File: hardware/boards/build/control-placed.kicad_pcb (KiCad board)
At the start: 4 copper layers, 177.9 x 107.5 mm, 108 parts

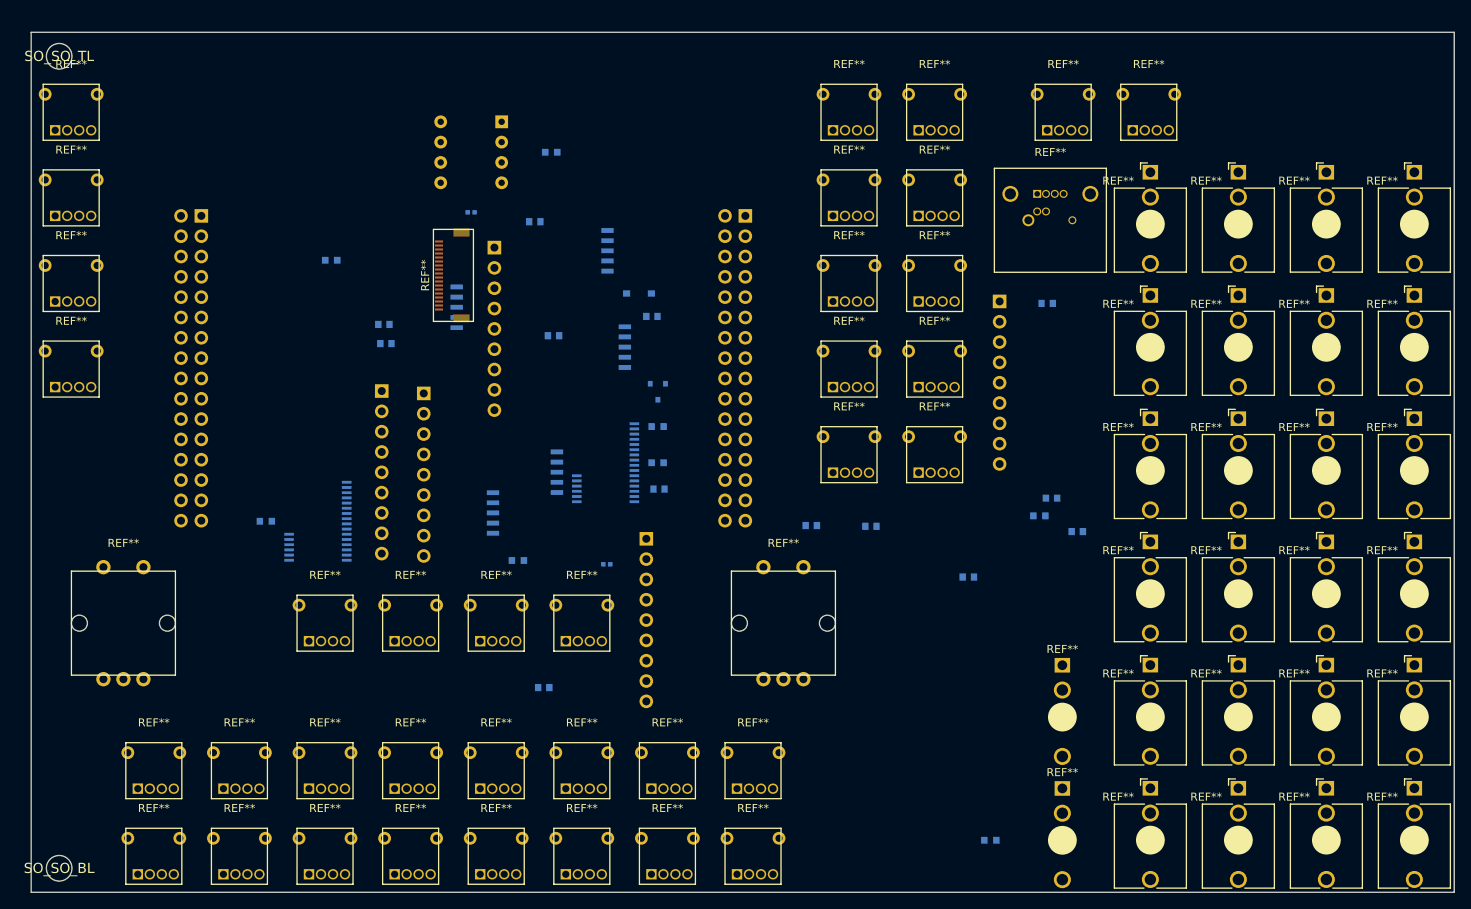
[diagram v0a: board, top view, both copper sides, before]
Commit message: Parts replaced
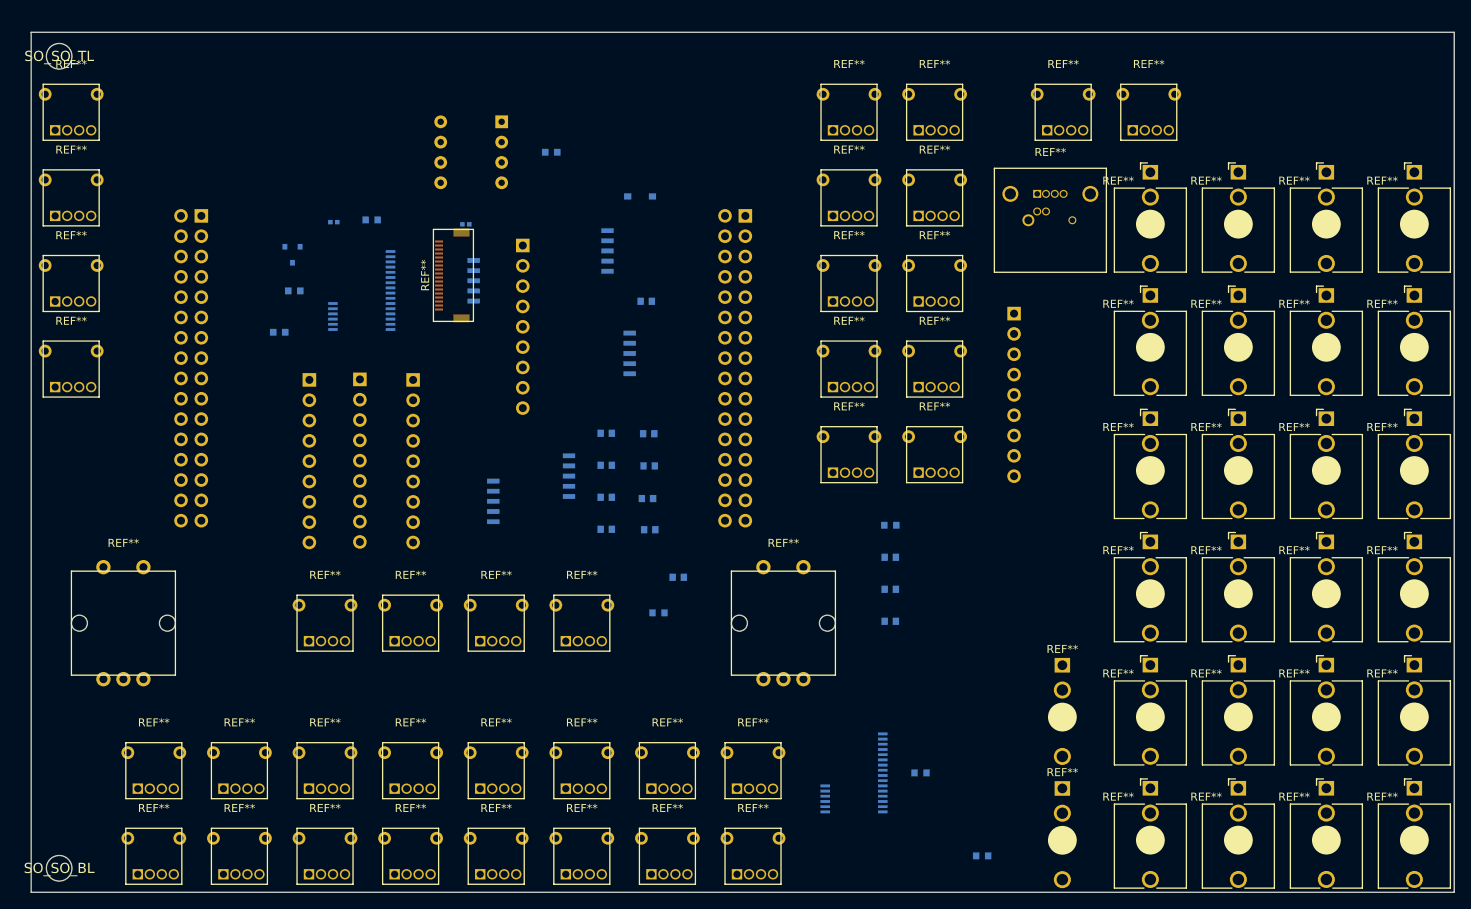
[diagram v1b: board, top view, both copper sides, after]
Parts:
- removed the REF** at (139.9, 63.7)
- removed the REF** at (161.9, 17.5)
- removed the REF** at (161.9, 79.1)
- removed the REF** at (139.9, 32.9)
- removed the REF** at (172.9, 48.3)
- removed the REF** at (139.9, 79.1)
- removed the REF** at (161.9, 94.5)
- removed the REF** at (150.9, 94.5)
- removed the REF** at (161.9, 32.9)
- removed the REF** at (139.9, 94.5)
- removed the REF** at (150.9, 63.7)
- removed the REF** at (172.9, 79.1)
- removed the REF** at (172.9, 17.5)
- removed the REF** at (139.9, 17.5)
- removed the REF** at (150.9, 32.9)
- removed the REF** at (150.9, 79.1)
- removed the REF** at (150.9, 48.3)
- removed the REF** at (161.9, 63.7)
- removed the REF** at (172.9, 32.9)
- removed the REF** at (161.9, 48.3)
- removed the REF** at (150.9, 17.5)
- removed the REF** at (172.9, 94.5)
- removed the REF** at (139.9, 48.3)
- removed the REF** at (121.1, 33.6)
- removed the REF** at (71.8, 53.8)
- removed the REF** at (71.5, 41.3)
- removed the REF** at (55.0, 62.0)
- removed the REF** at (57.9, 26.9)
- removed the REF** at (63.0, 56.9)
- removed the REF** at (76.9, 63.3)
- removed the REF** at (49.1, 45.1)
- removed the REF** at (50.5, 36.3)
- removed the REF** at (172.9, 63.7)
- removed the REF** at (35.8, 61.1)
- removed the REF** at (69.3, 29.2)
- removed the REF** at (43.8, 44.8)
- added REF**: WQP518MA, WQP518MA:WQP518MA, F.Cu at (150.9, 32.9)
- added REF**: WQP518MA, WQP518MA:WQP518MA, F.Cu at (139.9, 48.3)
- added REF**: WQP518MA, WQP518MA:WQP518MA, F.Cu at (139.9, 63.7)
- added REF**: WQP518MA, WQP518MA:WQP518MA, F.Cu at (172.9, 17.5)
- added REF**: WQP518MA, WQP518MA:WQP518MA, F.Cu at (139.9, 32.9)
- added REF**: WQP518MA, WQP518MA:WQP518MA, F.Cu at (150.9, 17.5)
- added REF**: WQP518MA, WQP518MA:WQP518MA, F.Cu at (139.9, 94.5)
- added REF**: WQP518MA, WQP518MA:WQP518MA, F.Cu at (172.9, 94.5)
- added REF**: WQP518MA, WQP518MA:WQP518MA, F.Cu at (150.9, 79.1)
- added REF**: WQP518MA, WQP518MA:WQP518MA, F.Cu at (161.9, 32.9)
- added REF**: WQP518MA, WQP518MA:WQP518MA, F.Cu at (161.9, 17.5)
- added REF**: WQP518MA, WQP518MA:WQP518MA, F.Cu at (161.9, 48.3)
- added REF**: WQP518MA, WQP518MA:WQP518MA, F.Cu at (139.9, 17.5)
- added REF**: WQP518MA, WQP518MA:WQP518MA, F.Cu at (172.9, 32.9)
- added REF**: WQP518MA, WQP518MA:WQP518MA, F.Cu at (161.9, 94.5)
- added REF**: WQP518MA, WQP518MA:WQP518MA, F.Cu at (172.9, 79.1)
- added REF**: WQP518MA, WQP518MA:WQP518MA, F.Cu at (172.9, 48.3)
- added REF**: WQP518MA, WQP518MA:WQP518MA, F.Cu at (150.9, 94.5)
- added REF**: WQP518MA, WQP518MA:WQP518MA, F.Cu at (161.9, 79.1)
- added REF**: WQP518MA, WQP518MA:WQP518MA, F.Cu at (161.9, 63.7)
- added REF**: WQP518MA, WQP518MA:WQP518MA, F.Cu at (150.9, 48.3)
- added REF**: WQP518MA, WQP518MA:WQP518MA, F.Cu at (172.9, 63.7)
- added REF**: WQP518MA, WQP518MA:WQP518MA, F.Cu at (139.9, 79.1)
- added REF**: WQP518MA, WQP518MA:WQP518MA, F.Cu at (150.9, 63.7)
- added REF**: SOIC-16, 74HC165D:SOIC-16, B.Cu at (69.3, 29.2)
- added REF**: SIP-9, ResistorNetwork9:SIP-9, B.Cu at (34.8, 43.5)
- added REF**: SOIC-16, 74HC165D:SOIC-16, B.Cu at (55.1, 60.5)
- added REF**: HTSSOP-32, TLC5947DAP:HTSSOP-32, B.Cu at (102.9, 92.6)
- added REF**: SIP-9, ResistorNetwork9:SIP-9, B.Cu at (41.1, 43.4)
- added REF**: SOIC-16, 74HC165D:SOIC-16, B.Cu at (64.5, 57.4)
- added REF**: SIP-9, ResistorNetwork9:SIP-9, B.Cu at (122.9, 35.2)
- added REF**: SOIC-16, 74HC165D:SOIC-16, B.Cu at (52.6, 33.0)
- added REF**: SOIC-16, 74HC165D:SOIC-16, B.Cu at (72.1, 42.1)
- added REF**: SIP-9, ResistorNetwork9:SIP-9, B.Cu at (47.7, 43.5)
- added REF**: HTSSOP-32, TLC5947DAP:HTSSOP-32, B.Cu at (41.3, 32.3)
- added REF**: SIP-9, ResistorNetwork9:SIP-9, B.Cu at (61.5, 26.7)
- C1, C10, C11, C12, C13, C2, C3, C4, C5, C7, C8, C9: value 0F -> 100nF
- C6: value 0F -> 10µF
- R1, R2: value 2000Ω -> 2kΩ
- R10: value 10000Ω -> 10kΩ
- R3: value 4700Ω -> 4.7kΩ
- R9: value 100000Ω -> 100kΩ
- moved C6 61.1 mm to (76.9, 33.6)
- moved R9 54.7 mm to (37.8, 23.7)
- moved R2 50.8 mm to (111.2, 92.6)
- moved C12 50.4 mm to (77.3, 62.2)
- moved REF** 48.8 mm to (32.7, 27.8)
- moved R8 48.8 mm to (31.0, 37.5)
- moved C2 37.3 mm to (107.4, 65.6)
- moved C3 35.8 mm to (77.2, 50.2)
- moved C7 33.1 mm to (71.9, 62.1)
- moved C10 32.8 mm to (80.9, 68.1)
- moved C9 31.5 mm to (107.4, 69.6)
- moved C1 31.5 mm to (71.9, 54.1)
- moved R1 29.0 mm to (32.9, 32.3)
- moved C8 27.9 mm to (71.9, 50.1)
- moved C13 25.0 mm to (71.9, 58.1)
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
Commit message: Update parts and placement algos
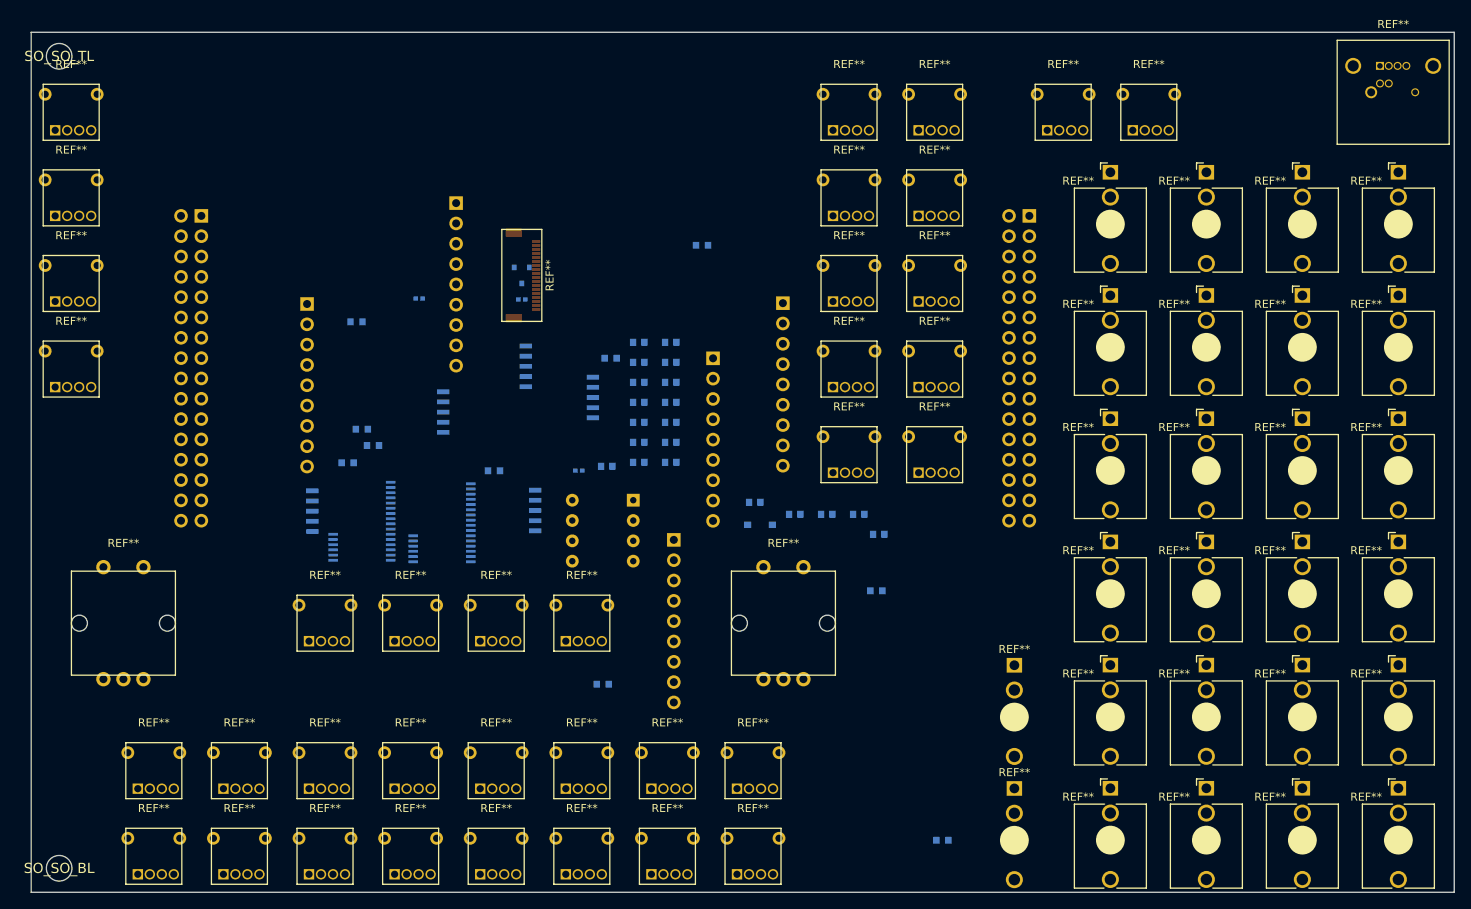
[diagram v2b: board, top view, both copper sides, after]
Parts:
- removed the REF** at (150.9, 32.9)
- removed the REF** at (139.9, 48.3)
- removed the REF** at (139.9, 63.7)
- removed the REF** at (172.9, 17.5)
- removed the REF** at (139.9, 32.9)
- removed the REF** at (150.9, 17.5)
- removed the REF** at (139.9, 94.5)
- removed the REF** at (172.9, 94.5)
- removed the REF** at (150.9, 79.1)
- removed the REF** at (161.9, 32.9)
- removed the REF** at (161.9, 17.5)
- removed the REF** at (128.9, 85.6)
- removed the REF** at (161.9, 48.3)
- removed the REF** at (139.9, 17.5)
- removed the REF** at (172.9, 32.9)
- removed the REF** at (161.9, 94.5)
- removed the REF** at (172.9, 79.1)
- removed the REF** at (172.9, 48.3)
- removed the REF** at (128.9, 101.0)
- removed the REF** at (150.9, 94.5)
- removed the REF** at (161.9, 79.1)
- removed the REF** at (161.9, 63.7)
- removed the REF** at (150.9, 48.3)
- removed the REF** at (172.9, 63.7)
- removed the REF** at (139.9, 79.1)
- removed the REF** at (150.9, 63.7)
- removed the REF** at (69.3, 29.2)
- removed the REF** at (34.8, 43.5)
- removed the REF** at (55.1, 60.5)
- removed the REF** at (102.9, 92.6)
- removed the REF** at (41.1, 43.4)
- removed the REF** at (64.5, 57.4)
- removed the REF** at (122.9, 35.2)
- removed the REF** at (52.6, 33.0)
- removed the REF** at (72.1, 42.1)
- removed the REF** at (47.7, 43.5)
- removed the REF** at (41.3, 32.3)
- removed the REF** at (61.5, 26.7)
- added C14: 100nF, YAGEO_CC0603KRX7R9BB104:C0603, B.Cu at (75.9, 51.2)
- added C15: 100nF, YAGEO_CC0603KRX7R9BB104:C0603, B.Cu at (103.4, 60.2)
- added C16: 100nF, YAGEO_CC0603KRX7R9BB104:C0603, B.Cu at (75.9, 41.2)
- added C17: 10µF, Samsung_Electro_Mechanics_CL10A106KP8NNNC:C0603, B.Cu at (75.9, 43.8)
- added C18: 10µF, Samsung_Electro_Mechanics_CL10A106KP8NNNC:C0603, B.Cu at (75.9, 46.2)
- added C19: 100nF, YAGEO_CC0603KRX7R9BB104:C0603, B.Cu at (75.9, 48.8)
- added C20: 100nF, YAGEO_CC0603KRX7R9BB104:C0603, B.Cu at (79.9, 53.8)
- added R11: 100kΩ, UNI_ROYAL_0402WGF1003TCE:R0402, B.Cu at (48.5, 33.3)
- added R12: 10kΩ, UNI_ROYAL_0603WAF1002T5E:R0603, B.Cu at (72.4, 40.8)
- added R13: 47kΩ, UNI_ROYAL_0603WAF4702T5E:R0603, B.Cu at (83.9, 26.6)
- added REF**: WQP518MA, WQP518MA:WQP518MA, F.Cu at (170.9, 32.9)
- added REF**: WQP518MA, WQP518MA:WQP518MA, F.Cu at (158.9, 79.1)
- added REF**: WQP518MA, WQP518MA:WQP518MA, F.Cu at (158.9, 32.9)
- added REF**: WQP518MA, WQP518MA:WQP518MA, F.Cu at (134.9, 79.1)
- added REF**: WQP518MA, WQP518MA:WQP518MA, F.Cu at (146.9, 32.9)
- added REF**: WQP518MA, WQP518MA:WQP518MA, F.Cu at (146.9, 94.5)
- added REF**: WQP518MA, WQP518MA:WQP518MA, F.Cu at (158.9, 48.3)
- added REF**: WQP518MA, WQP518MA:WQP518MA, F.Cu at (134.9, 17.5)
- added REF**: WQP518MA, WQP518MA:WQP518MA, F.Cu at (146.9, 79.1)
- added REF**: WQP518MA, WQP518MA:WQP518MA, F.Cu at (134.9, 94.5)
- added REF**: PJ366ST, PJ366ST:PJ366ST, F.Cu at (122.9, 101.0)
- added REF**: WQP518MA, WQP518MA:WQP518MA, F.Cu at (170.9, 17.5)
- added REF**: WQP518MA, WQP518MA:WQP518MA, F.Cu at (134.9, 48.3)
- added REF**: WQP518MA, WQP518MA:WQP518MA, F.Cu at (170.9, 63.7)
- added REF**: WQP518MA, WQP518MA:WQP518MA, F.Cu at (146.9, 63.7)
- added REF**: WQP518MA, WQP518MA:WQP518MA, F.Cu at (170.9, 79.1)
- added REF**: WQP518MA, WQP518MA:WQP518MA, F.Cu at (158.9, 94.5)
- added REF**: WQP518MA, WQP518MA:WQP518MA, F.Cu at (170.9, 48.3)
- added REF**: WQP518MA, WQP518MA:WQP518MA, F.Cu at (158.9, 17.5)
- added REF**: WQP518MA, WQP518MA:WQP518MA, F.Cu at (146.9, 17.5)
- added REF**: PJ366ST, PJ366ST:PJ366ST, F.Cu at (122.9, 85.6)
- added REF**: WQP518MA, WQP518MA:WQP518MA, F.Cu at (134.9, 32.9)
- added REF**: WQP518MA, WQP518MA:WQP518MA, F.Cu at (146.9, 48.3)
- added REF**: WQP518MA, WQP518MA:WQP518MA, F.Cu at (158.9, 63.7)
- added REF**: SOIC-16, 74HC165D:SOIC-16, B.Cu at (48.8, 49.4)
- added REF**: HTSSOP-32, TLC5947DAP:HTSSOP-32, B.Cu at (51.4, 61.3)
- added REF**: SOIC-16, 74HC165D:SOIC-16, B.Cu at (59.1, 43.7)
- added REF**: SIP-9, ResistorNetwork9:SIP-9, B.Cu at (53.1, 21.4)
- added REF**: HTSSOP-32, TLC5947DAP:HTSSOP-32, B.Cu at (41.3, 61.1)
- added REF**: SIP-9, ResistorNetwork9:SIP-9, B.Cu at (80.3, 63.4)
- added REF**: SIP-9, ResistorNetwork9:SIP-9, B.Cu at (85.2, 40.8)
- added REF**: SIP-9, ResistorNetwork9:SIP-9, B.Cu at (94.0, 33.9)
- added REF**: SOIC-16, 74HC165D:SOIC-16, B.Cu at (60.3, 61.7)
- added REF**: SOIC-16, 74HC165D:SOIC-16, B.Cu at (67.5, 47.6)
- added REF**: WQP518MA, WQP518MA:WQP518MA, F.Cu at (134.9, 63.7)
- added REF**: SOIC-16, 74HC165D:SOIC-16, B.Cu at (32.4, 61.8)
- added REF**: SIP-9, ResistorNetwork9:SIP-9, B.Cu at (34.5, 34.0)
- added REF**: WQP518MA, WQP518MA:WQP518MA, F.Cu at (170.9, 94.5)
- R1: value 2kΩ -> 10kΩ; footprint UNI_ROYAL_0603WAF2001T5E:R0603 -> UNI_ROYAL_0603WAF1002T5E:R0603
- R10: value 10kΩ -> 33Ω; footprint UNI_ROYAL_0603WAF1002T5E:R0603 -> UNI_ROYAL_0402WGF330JTCE:R0402
- R3: value 4.7kΩ -> 2kΩ; footprint UNI_ROYAL_0402WGF4701TCE:R0402 -> UNI_ROYAL_0603WAF2001T5E:R0603
- R4: value 220Ω -> 4.7kΩ; footprint UNI_ROYAL_0603WAF2200T5E:R0603 -> UNI_ROYAL_0402WGF4701TCE:R0402
- R7: value 470Ω -> 220Ω; footprint UNI_ROYAL_0603WAF4700T5E:R0603 -> UNI_ROYAL_0603WAF2200T5E:R0603
- R8: value 100Ω -> 1kΩ; footprint UNI_ROYAL_0603WAF1000T5E:R0603 -> UNI_ROYAL_0603WAF1001T5E:R0603
- R9: value 100kΩ -> 100Ω; footprint UNI_ROYAL_0402WGF1003TCE:R0402 -> UNI_ROYAL_0603WAF1000T5E:R0603
- moved R2 82.0 mm to (41.3, 49.6)
- moved R7 64.8 mm to (71.5, 81.5)
- moved R10 54.0 mm to (61.3, 33.4)
- moved REF** 50.1 mm to (71.5, 62.3)
- moved REF** 45.7 mm to (170.2, 7.50)
- moved R6 45.5 mm to (113.9, 101.0)
- moved C11 44.4 mm to (79.9, 38.8)
- moved REF** 43.7 mm to (91.1, 61.6)
- moved R4 39.9 mm to (68.5, 54.8)
- moved C9 38.6 mm to (71.9, 54.2)
- moved C8 36.3 mm to (105.9, 62.8)
- moved R5 35.7 mm to (105.6, 69.8)
- moved REF** 35.5 mm to (123.5, 42.0)
- moved C2 35.1 mm to (79.9, 43.8)
- moved C6 32.5 mm to (95.4, 60.2)
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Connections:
- C10 pad 1: c_sd-power-hv -> c_cv_c-power-hv
- C11 pad 1: c_sd-power-hv -> c_cv_d-power-hv
- C12 pad 1: c_sd-power-hv -> c_lcd_rst-power-hv
- C8 pad 1: c_lcd_rst-power-hv -> c_cv_a-power-hv
- C9 pad 1: c_sd-power-hv -> c_cv_b-power-hv
- R1 pad 1: IREF -> c_sd-power-hv
- R1 pad 2: lv -> BLANK
- R10 pad 2: c_lcd_rst-power-hv -> 10
- R2 pad 1: leds-IREF -> IREF
- R3 pad 1: VE -> leds-IREF
- R4 pad 1: TIP -> VE
- R4 pad 2: CATHODE -> lv
- R5 pad 1: c_sd-power-hv -> TIP
- R5 pad 2: RING -> CATHODE
- R6 pad 1: midi_tx -> hv
- R6 pad 2: midi-TIP -> RING
- R7 pad 1: c_sd-power-hv -> midi_tx
- R7 pad 2: midi_rx -> midi-TIP
- R8 pad 1: lcd_bl -> c_sd-power-hv
- R8 pad 2: gate -> midi_rx
- R9 pad 1: gate -> lcd_bl
- R9 pad 2: lv -> gate
- REF** pad 10: c_sd-power-hv -> 10
- REF** pad 10: cv_a -> c_cv_c-power-hv
- REF** pad 11: cv_b -> c_cv_d-power-hv
- REF** pad 12: cv_c -> lv
- REF** pad 13: cv_d -> gate1
- REF** pad 14: gate1 -> gate2
- REF** pad 15: gate2 -> gate3
- REF** pad 16: gate3 -> gate4
- REF** pad 17: gate4 -> lv
- REF** pad 22: vel1 -> lv
- REF** pad 23: vel2 -> vel1
- REF** pad 24: vel3 -> vel2
- REF** pad 25: vel4 -> vel3
- REF** pad 26: mod1 -> vel4
- REF** pad 27: mod2 -> lv
- REF** pad 28: mod3 -> mod1
- REF** pad 29: mod4 -> mod2
- REF** pad 3: A-1 -> clk_in
- REF** pad 30: hv -> mod3
- REF** pad 31: lv -> mod4
- REF** pad 4: B-1 -> clk_out
- REF** pad 5: enc_b_sw -> rst_in
- REF** pad 6: clk_in -> rst_out
- REF** pad 7: rst_in -> lv
- REF** pad 8: clk_out -> c_cv_a-power-hv
- REF** pad 9: rst_out -> c_cv_b-power-hv
- REF** pad 19: 19 -> A-1
- REF** pad 20: 20 -> B-1
- REF** pad 21: 21 -> enc_b_sw
